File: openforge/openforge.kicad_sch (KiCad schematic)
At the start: 0 parts

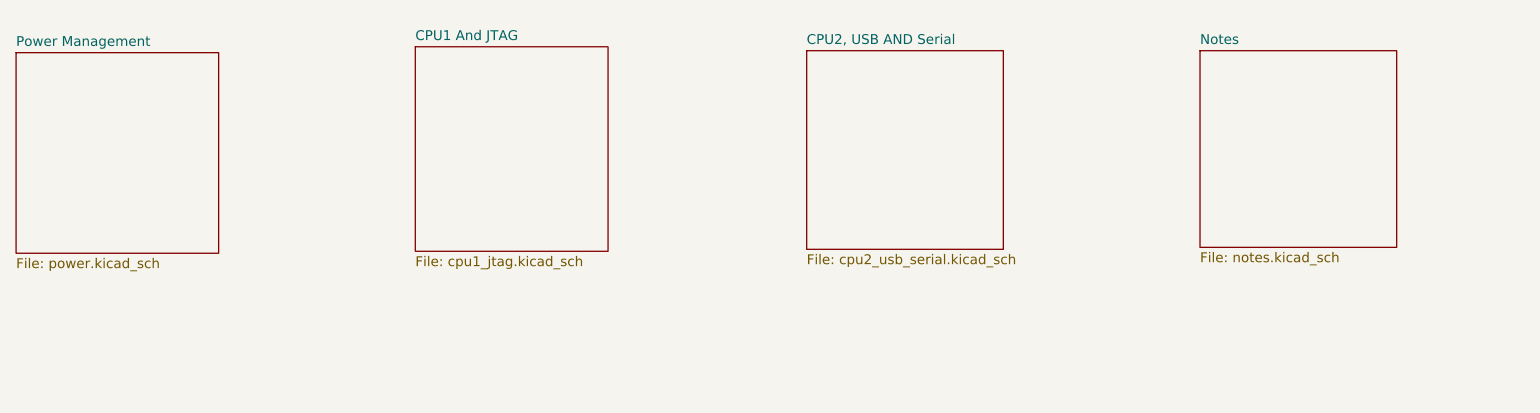
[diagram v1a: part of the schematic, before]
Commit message: Completed footprint association. Partially placed top side components on PCB
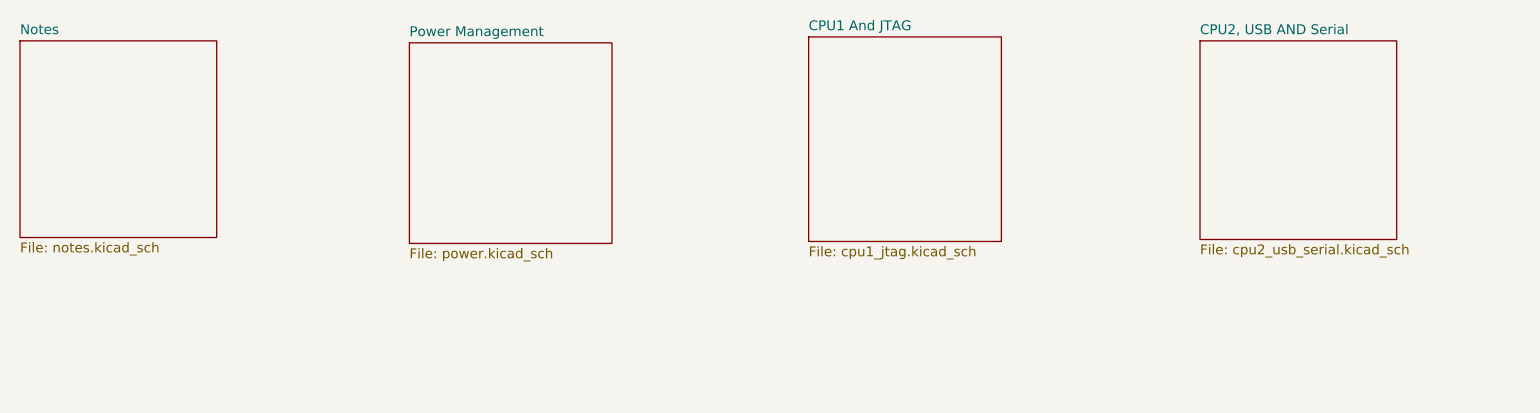
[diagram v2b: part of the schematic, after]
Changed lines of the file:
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@@
 	)
 	(sheet
-		(at 101.854 24.892)
+		(at 152.654 23.622)
 		(size 24.892 26.416)
 		(fields_autoplaced yes)
@@
 		)
 		(property "Sheetname" "CPU1 And JTAG"
-			(at 101.854 24.1804 0)
+			(at 152.654 22.9104 0)
 			(effects
 				(font
@@
 		)
 		(property "Sheetfile" "cpu1_jtag.kicad_sch"
-			(at 101.854 51.8926 0)
+			(at 152.654 50.6226 0)
 			(effects
 				(font
@@
 	)
 	(sheet
-		(at 203.2 25.4)
+		(at 50.8 24.13)
 		(size 25.4 25.4)
 		(fields_autoplaced yes)
@@
 		)
 		(property "Sheetname" "Notes"
-			(at 203.2 24.6884 0)
+			(at 50.8 23.4184 0)
 			(effects
 				(font
@@
 		)
 		(property "Sheetfile" "notes.kicad_sch"
-			(at 203.2 51.3846 0)
+			(at 50.8 50.1146 0)
 			(effects
 				(font
@@
 	)
 	(sheet
-		(at 152.4 25.4)
+		(at 203.2 24.13)
 		(size 25.4 25.654)
 		(fields_autoplaced yes)
@@
 		)
 		(property "Sheetname" "CPU2, USB AND Serial"
-			(at 152.4 24.6884 0)
+			(at 203.2 23.4184 0)
 			(effects
 				(font
@@
 		)
 		(property "Sheetfile" "cpu2_usb_serial.kicad_sch"
-			(at 152.4 51.6386 0)
+			(at 203.2 50.3686 0)
 			(effects
 				(font
@@
 	)
 	(sheet
-		(at 50.292 25.654)
+		(at 101.092 24.384)
 		(size 26.162 25.908)
 		(fields_autoplaced yes)
@@
 		)
 		(property "Sheetname" "Power Management"
-			(at 50.292 24.9424 0)
+			(at 101.092 23.6724 0)
 			(effects
 				(font
@@
 		)
 		(property "Sheetfile" "power.kicad_sch"
-			(at 50.292 52.1466 0)
-			(effects
-				(font
+			(at 101.092 50.8766 0)
+			(effects
+				(font
